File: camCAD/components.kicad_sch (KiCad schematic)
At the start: 11 parts, among them J4 ILI9341_Display_Header

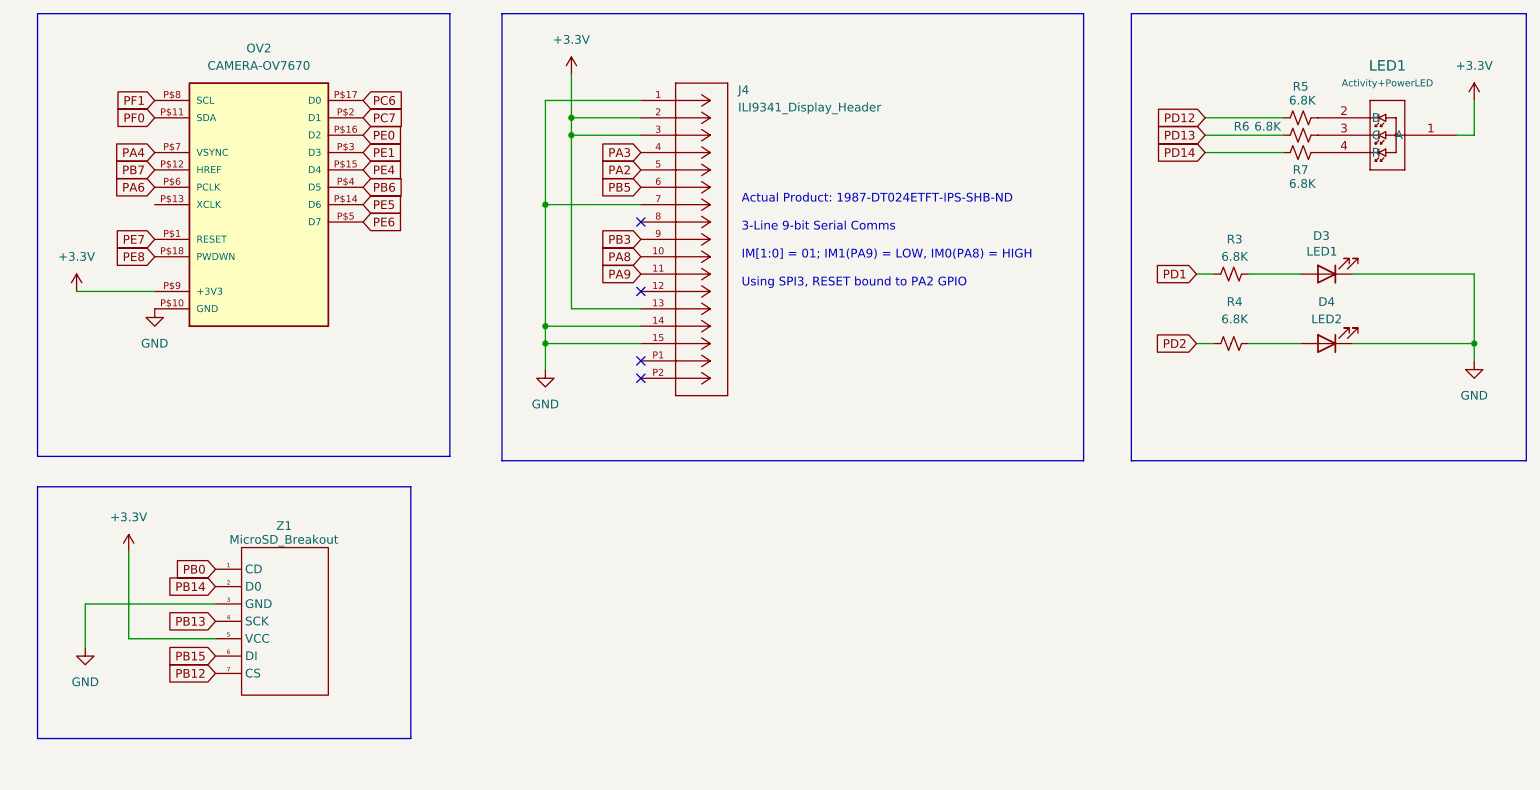
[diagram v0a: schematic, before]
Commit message: Added battery to HardwareNotes.md, some touch ups on schematic
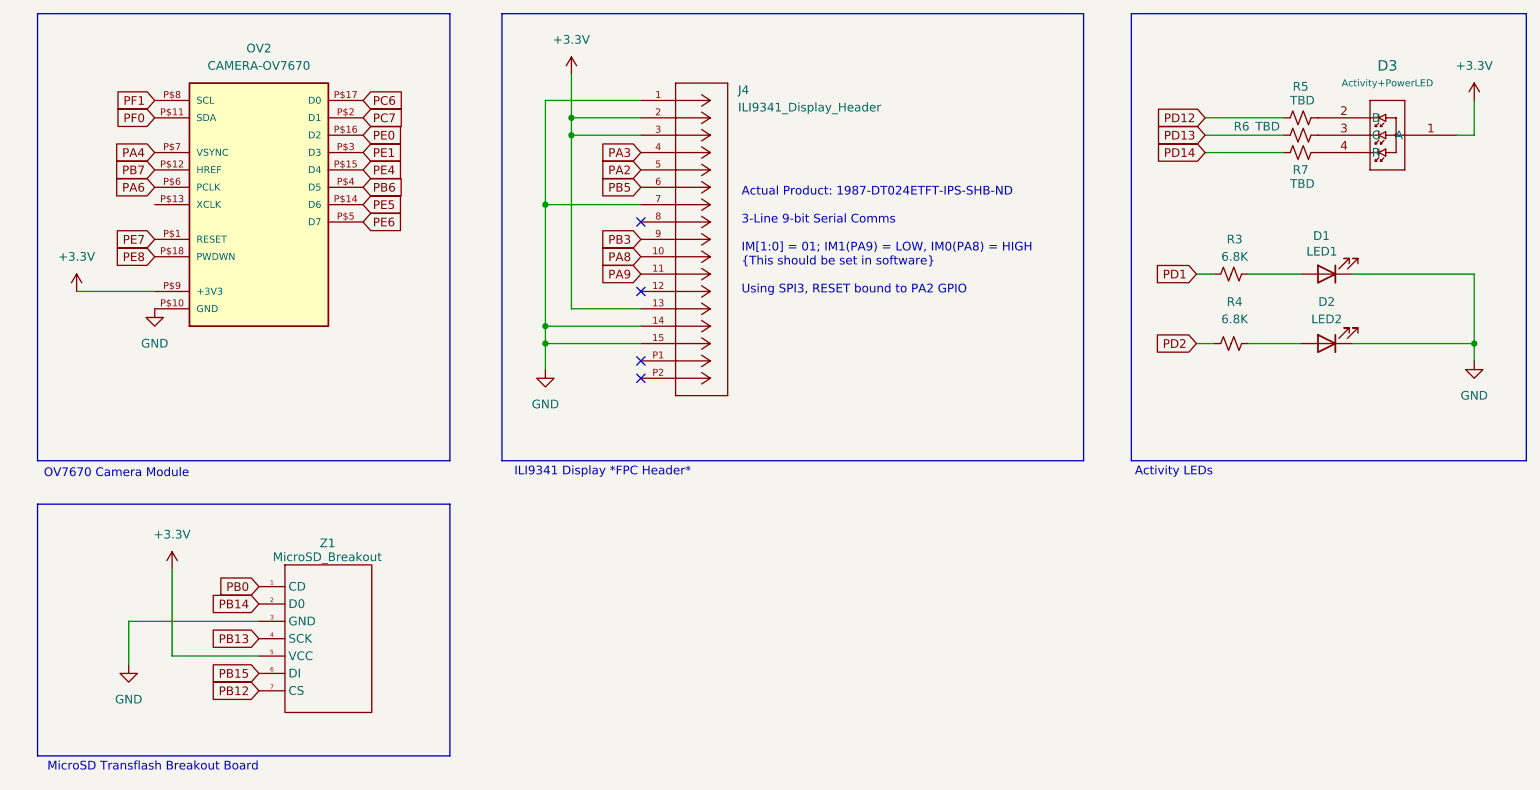
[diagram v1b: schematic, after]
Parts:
- R5, R6, R7: value 6.8K -> TBD
- renumbered D3 to D1, D4 to D2, LED1 to D3
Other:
- note added: "Activity LEDs"
- note added: "Actual Product: 1987-DT024ETFT-IPS-SHB-ND 3-Line 9-bit Serial Comms IM[1:0] = 01; IM1(PA9) = LOW, IM0(PA8) = HIGH {This should be set in software} Using SPI3, RESET bound to PA2 GPIO"
- note added: "ILI9341 Display *FPC Header*"
- note added: "MicroSD Transflash Breakout Board"
- note added: "OV7670 Camera Module"
- note removed: "Actual Product: 1987-DT024ETFT-IPS-SHB-ND 3-Line 9-bit Serial Comms IM[1:0] = 01; IM1(PA9) = LOW, IM0(PA8) = HIGH Using SPI3, RESET bound to PA2 GPIO"
- moved on the sheet: Z1
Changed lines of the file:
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@@
 	(generator "eeschema")
 	(generator_version "10.0")
-	(paper "A4")
+	(paper "User" 254 203.2)
 	(rectangle
 		(start 17.145 16.51)
-		(end 77.47 81.28)
+		(end 77.47 81.915)
 		(stroke
 			(width 0)
@@
 	)
 	(rectangle
-		(start 17.145 85.725)
-		(end 71.755 122.555)
+		(start 17.145 88.265)
+		(end 77.47 125.095)
 		(stroke
 			(width 0)
@@
 		)
 	)
-	(text "\nActual Product: 1987-DT024ETFT-IPS-SHB-ND\n\n3-Line 9-bit Serial Comms\n\nIM[1:0] = 01; IM1(PA9) = LOW, IM0(PA8) = HIGH\n\nUsing SPI3, RESET bound to PA2 GPIO"
+	(text "ILI9341 Display *FPC Header*"
+		(exclude_from_sim no)
+		(at 99.822 83.566 0)
+		(effects
+			(font
+				(size 1.27 1.27)
+			)
+		)
+	)
+	(text "MicroSD Transflash Breakout Board\n"
+		(exclude_from_sim no)
+		(at 34.036 126.746 0)
+		(effects
+			(font
+				(size 1.27 1.27)
+			)
+		)
+	)
+	(text "Activity LEDs"
+		(exclude_from_sim no)
+		(at 183.388 83.566 0)
+		(effects
+			(font
+				(size 1.27 1.27)
+			)
+		)
+	)
+	(text "\nActual Product: 1987-DT024ETFT-IPS-SHB-ND\n\n3-Line 9-bit Serial Comms\n\nIM[1:0] = 01; IM1(PA9) = LOW, IM0(PA8) = HIGH \n{This should be set in software}\n\nUsing SPI3, RESET bound to PA2 GPIO"
 		(exclude_from_sim no)
 		(at 120.142 48.768 0)
@@
 			)
 			(justify left)
+		)
+	)
+	(text "OV7670 Camera Module"
+		(exclude_from_sim no)
+		(at 28.702 83.82 0)
+		(effects
+			(font
+				(size 1.27 1.27)
+			)
 		)
 	)
@@
 	(wire
 		(pts
-			(xy 24.13 102.87) (xy 24.13 109.22)
+			(xy 30.48 105.41) (xy 30.48 111.76)
 		)
 		(stroke
@@
 	(wire
 		(pts
-			(xy 30.48 95.25) (xy 30.48 107.95)
+			(xy 36.83 97.79) (xy 36.83 110.49)
 		)
 		(stroke
@@
 	(wire
 		(pts
-			(xy 43.18 107.95) (xy 30.48 107.95)
+			(xy 49.53 110.49) (xy 36.83 110.49)
 		)
 		(stroke
@@
 	(wire
 		(pts
-			(xy 43.18 102.87) (xy 24.13 102.87)
+			(xy 49.53 105.41) (xy 30.48 105.41)
 		)
 		(stroke
@@
 	(global_label "PB0"
 		(shape input)
-		(at 43.18 97.79 180)
+		(at 49.53 100.33 180)
 		(fields_autoplaced yes)
 		(effects
@@
 		)
 		(property "Intersheetrefs" "${INTERSHEET_REFS}"
-			(at 36.4453 97.79 0)
+			(at 42.7953 100.33 0)
 			(hide yes)
 			(show_name no)
@@
 	(global_label "PB14"
 		(shape input)
-		(at 43.18 100.33 180)
+		(at 49.53 102.87 180)
 		(fields_autoplaced yes)
 		(effects
@@
 		)
 		(property "Intersheetrefs" "${INTERSHEET_REFS}"
-			(at 35.2358 100.33 0)
+			(at 41.5858 102.87 0)
 			(hide yes)
 			(show_name no)
@@
 	(global_label "PB13"
 		(shape input)
-		(at 43.18 105.41 180)
+		(at 49.53 107.95 180)
 		(fields_autoplaced yes)
 		(effects
@@
 		)
 		(property "Intersheetrefs" "${INTERSHEET_REFS}"
-			(at 35.2358 105.41 0)
+			(at 41.5858 107.95 0)
 			(hide yes)
 			(show_name no)
@@
 	(global_label "PB15"
 		(shape input)
-		(at 43.18 110.49 180)
+		(at 49.53 113.03 180)
 		(fields_autoplaced yes)
 		(effects
@@
 		)
 		(property "Intersheetrefs" "${INTERSHEET_REFS}"
-			(at 35.2358 110.49 0)
+			(at 41.5858 113.03 0)
 			(hide yes)
 			(show_name no)
@@
 	(global_label "PB12"
 		(shape input)
-		(at 43.18 113.03 180)
+		(at 49.53 115.57 180)
 		(fields_autoplaced yes)
 		(effects
@@
 		)
 		(property "Intersheetrefs" "${INTERSHEET_REFS}"
-			(at 35.2358 113.03 0)
+			(at 41.5858 115.57 0)
 			(hide yes)
 			(show_name no)
@@
 	(symbol
 		(lib_id "power:GND")
-		(at 24.13 109.22 0)
+		(at 30.48 111.76 0)
 		(unit 1)
 		(body_style 1)
@@
 		(fields_autoplaced yes)
 		(property "Reference" "#PWR023"
-			(at 24.13 115.57 0)
+			(at 30.48 118.11 0)
 			(hide yes)
 			(show_name no)
@@
 		)
 		(property "Value" "GND"
-			(at 24.13 114.3 0)
+			(at 30.48 116.84 0)
 			(show_name no)
 			(do_not_autoplace no)
@@
 		)
 		(property "Footprint" ""
-			(at 24.13 109.22 0)
+			(at 30.48 111.76 0)
 			(hide yes)
 			(show_name no)
@@
 		)
 		(property "Datasheet" ""
-			(at 24.13 109.22 0)
+			(at 30.48 111.76 0)
 			(hide yes)
 			(show_name no)
@@
 		)
 		(property "Description" "Power symbol creates a global label with name \"GND\" , ground"
-			(at 24.13 109.22 0)
+			(at 30.48 111.76 0)
 			(hide yes)
 			(show_name no)
@@
 		(dnp no)
 		(fields_autoplaced yes)
-		(property "Reference" "LED1"
+		(property "Reference" "D3"
 			(at 214.63 24.13 0)
 			(show_name no)
@@
 			(project "camCAD"
 				(path "/e2824ea6-9024-4cee-b80c-5fefbc7112d7/6a2215d2-deaa-4e55-8021-5c3b01265060"
-					(reference "LED1")
+					(reference "D3")
 					(unit 1)
 				)
@@
 		(in_pos_files yes)
 		(dnp no)
-		(property "Reference" "D3"
+		(property "Reference" "D1"
 			(at 204.978 49.022 0)
 			(show_name no)
@@
 			(project "camCAD"
 				(path "/e2824ea6-9024-4cee-b80c-5fefbc7112d7/6a2215d2-deaa-4e55-8021-5c3b01265060"
-					(reference "D3")
+					(reference "D1")
 					(unit 1)
 				)
@@
 			)
 		)
-		(property "Value" "6.8K"
+		(property "Value" "TBD"
 			(at 202.184 41.402 90)
 			(show_name no)
@@
 	(symbol
 		(lib_id "1_MicroSD:MicroSD_BREA")
-		(at 53.34 105.41 0)
+		(at 59.69 107.95 0)
 		(unit 1)
 		(body_style 1)
@@
 		(dnp no)
 		(property "Reference" "Z1"
-			(at 52.07 91.44 0)
+			(at 58.42 93.98 0)
 			(show_name no)
 			(do_not_autoplace no)
@@
 		)
 		(property "Value" "MicroSD_Breakout"
-			(at 45.212 93.472 0)
+			(at 51.562 96.012 0)
 			(show_name no)
 			(do_not_autoplace no)
@@
 		)
 		(property "Footprint" ""
-			(at 53.34 105.41 0)
+			(at 59.69 107.95 0)
 			(hide yes)
 			(show_name no)
@@
 		)
 		(property "Datasheet" ""
-			(at 53.34 105.41 0)
+			(at 59.69 107.95 0)
 			(hide yes)
 			(show_name no)
@@
 		)
 		(property "Description" ""
-			(at 53.34 105.41 0)
+			(at 59.69 107.95 0)
 			(hide yes)
 			(show_name no)
@@
 			)
 		)
-		(property "Value" "6.8K"
+		(property "Value" "TBD"
 			(at 202.184 29.21 90)
 			(show_name no)
@@
 	(symbol
 		(lib_id "power:+3.3V")
-		(at 30.48 95.25 0)
+		(at 36.83 97.79 0)
 		(unit 1)
 		(body_style 1)
@@
 		(fields_autoplaced yes)
 		(property "Reference" "#PWR024"
-			(at 30.48 99.06 0)
+			(at 36.83 101.6 0)
 			(hide yes)
 			(show_name no)
@@
 		)
 		(property "Value" "+3.3V"
-			(at 30.48 90.17 0)
+			(at 36.83 92.71 0)
 			(show_name no)
 			(do_not_autoplace no)
@@
 		)
 		(property "Footprint" ""
-			(at 30.48 95.25 0)
+			(at 36.83 97.79 0)
 			(hide yes)
 			(show_name no)
@@
 		)
 		(property "Datasheet" ""
-			(at 30.48 95.25 0)
+			(at 36.83 97.79 0)
 			(hide yes)
 			(show_name no)
@@
 		)
 		(property "Description" "Power symbol creates a global label with name \"+3.3V\""
-			(at 30.48 95.25 0)
+			(at 36.83 97.79 0)
 			(hide yes)
 			(show_name no)
@@
 			)
 		)
-		(property "Value" "6.8K"
+		(property "Value" "TBD"
 			(at 197.104 33.02 90)
 			(show_name no)
@@
 		(in_pos_files yes)
 		(dnp no)
-		(property "Reference" "D4"
+		(property "Reference" "D2"
 			(at 205.74 58.674 0)
 			(show_name no)
@@
 			(project "camCAD"
 				(path "/e2824ea6-9024-4cee-b80c-5fefbc7112d7/6a2215d2-deaa-4e55-8021-5c3b01265060"
-					(reference "D4")
+					(reference "D2")
 					(unit 1)
 				)

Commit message: Adding charging functionality
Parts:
- added R1: R_US, symbol Device:R_US
- added SW2: SW_Push, symbol Switch:SW_Push
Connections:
- net +3.3V: now also SW2.1
- net GND: now also R1.2
- new net BOOT0: R1.1, SW2.2
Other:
- note added: "Bootloader mode switch"
- title: (none) -> Component Schematics
- moved on the sheet: Z1
